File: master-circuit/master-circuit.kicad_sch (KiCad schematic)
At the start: 114 parts, among them U6 20nF 5%

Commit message: Finish master controller circuit, arrange chips on the board.
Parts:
- removed C17, C18, C27, C28, C29: 100nF, Library:C0603, symbol Library:CC0603KRX7R9BB104 Capacitor 100nF
- removed C36, C37, C38, C39: 1uF, Library:C0603, symbol Library:CL10A105KB8NNNC Capacitor 1uF
- removed D5: ~, Library:SOT-23-3_L3.0-W1.7-P0.95-LS2.9-BR, symbol Library:PSM712-LF-T7 ETV/ESD Diodes
- removed FPC1: ~, Library:FPC-SMD_20P-P0.50_XUNPU_FPC-05F-20PH20, symbol Library:FPC-05F-20PH20 Connector 6P 0.5mm spacing FPC
- removed Q1, Q2, Q3, Q4: ~, Library:WDFN-5_L3.1-W3.1-P0.65-BL_1, symbol Library:40N06D MOSFET N-Channel 40A
- removed U10, U11, U12, U13, U14, U15, U16, U9: ~, Library:DHVQFN-16_L3.5-W2.5-P0.50-BL-EP, symbol Library:RS595SXTQW16 Shift Register
- removed U2, U7: ~, Library:WLCSP-6_L1.2-W0.8-P0.40-TL, symbol Library:TCK420G,L3F Gate driver (high side)
- removed U20: ~, Library:VSSOP-10_L3.0-W3.0-P0.50-LS4.9-BL, symbol Library:INA2181A1IDGSR Current amplifier 2x 20V/V
- added C17: 10uF, Library:C1206, symbol Library:CL31A106KBHNNNE Capacitor 10uF
- added C18: 1uF, Library:C0603, symbol Library:CL10A105KB8NNNC Capacitor 1uF
- added C27, C28: 330pF, Library:C0603, symbol Library:CL10C331JB8NNNC Capacitor 330pF
- added D8: ~, Library:SOT-23-3_L3.0-W1.7-P0.95-LS2.9-BR, symbol Library:PSM712-LF-T7 ETV/ESD Diodes
- added D9: ~, Library:SOD-123_L2.7-W1.6-LS3.7-RD-1, symbol Library:B5819W_C8598 Schottky diode
- added I2C1, I2C2: ~, Library:FPC-SMD_6P-P0.50_XUNPU_FPC-05F-6PH20, symbol Library:FPC-05F-6PH20 Connector 6P 0.5mm spacing FPC
- added R38: 5mΩ, Library:R2512 Shunt with Kelvin connections, symbol Library:RLP25FEGMR005 Shunt resistor 5mΩ 1%
- added R39: 1.5kΩ, Library:R0603, symbol Library:0603WAF1501T5E Resistor 1.5kΩ
- added R40: 20kΩ, Library:R0603, symbol Library:0603WAF2002T5E Resistor 20kΩ
- added R41: 47kΩ, Library:R0603, symbol Library:0603WAF4702T5E Resistor 47kΩ
- added U10: ~, Library:QFN-28_L5.0-W5.0-P0.50-TL-EP3.3, symbol Library:CP2102N-A02-GQFN28R USB to UART converter
- added U11: ~, Library:TSSOP-20_L6.5-W4.4-P0.65-LS6.4-BL, symbol Library:INA4181A1IPWR Current amplifier
- added U9: ~, Library:QFN-14_L2.5-W2.5-P0.50-TL-EP1.4, symbol Library:HUSB311BLA USB dual role PD
- added USB2: ~, Library:USB-C-SMD_TYPE-C16PIN, symbol Library:TYPE-C16PIN USB connector
- H1, H2, U19: now not fitted
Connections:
- net +Probe-1: now also U11.4 (IN+1)
- net +Probe-2: now also U11.6 (IN+2)
- net -Probe-1: now also U11.3 (IN±1)
- net -Probe-2: now also U11.7 (IN±2)
- net 3V3: now also C17.2, I2C1.2, I2C2.2, R39.1, U10.6 (VDD), U10.7 (VREGIN), U9.12 (VCONN), U9.13 (VCONN), U9.3 (VDD), U9.4 (VDD)
- net 3V3A: now also U11.5 (VS)
- net BATTERY_CURRENT: now also U11.8 (OUT2)
- net FSPICLK/SPI2_CLK: now also U8.11 (SRCLK)
- net FSPICS0/MEMORY_CS: now also D4.1 (A1)
- net GND: now also C15.1, C16.1, C25.1, C26.1, U8.17 (EP), U8.8 (GND), C17.1, C18.2, C27.1, C28.1, D8.3 (K), I2C1.1, I2C2.1, R41.2, U10.29 (EP), U10.3 (GND), U11.16 (GND), U9.15 (EP), U9.9 (GND), USB2.1 (SHELL), USB2.2 (SHELL), USB2.3 (SHELL), USB2.4 (SHELL), USB2.A1B12 (GND), USB2.B1A12 (GND)
- net I2C1_SCL: now also I2C1.4
- net I2C1_SDA: now also I2C1.3
- net I2C2_SCL: now also I2C2.4, U9.6 (SCL)
- net I2C2_SDA: now also I2C2.3, U9.7 (SDA)
- net REFERENCE: now also U11.1 (REF1), U11.12 (REF3), U11.20 (REF4), U11.9 (REF2)
- net RX: now also U10.26 (TXD)
- net SPI3_CLK: no longer U8.11 (SRCLK)
- net SPI3_MOSI: no longer U8.14 (SER)
- net STATUS_LED: now also U1.28 (IO35); no longer U1.12 (IO8)
- net TX: now also U10.25 (RXD)
- net VBUS_CURRENT: now also U11.2 (OUT1)
- net at C21.2, C22.2, D1.1 (-)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: now also D9.1 (-)
- net at CARD1.8 (DAT1(RSV)), R12.1: no longer D4.1 (A1)
- net I2C1_BOOT0/STOP: now reaches U8.1 (Q1)
- net I2C1_BOOT0/STOP: now also I2C1.6
- net I2C1_NRST: now reaches U8.15 (Q0)
- net I2C1_NRST: now also I2C1.5
- net I2C2_NRST: now reaches U8.2 (Q2)
- net I2C2_NRST: now also I2C2.5
- net I2C2_BOOT0/STOP: now reaches U8.3 (Q3)
- net I2C2_BOOT0/STOP: now also I2C2.6
- net SENSOR_NRST: now reaches U8.4 (Q4)
- net SENSOR_NRST: now also USB2.A8 (SBU1)
- net SENSOR_BOOT0/STOP: now reaches U8.5 (Q5)
- net SENSOR_BOOT0/STOP: now also USB2.B8 (SBU2)
- net CONNECT_SENSORS_5V: now reaches U8.6 (Q6)
- net CONNECT_SENSORS_VCC: now reaches U8.7 (Q7)
- net IMU_INTERRUPT: no longer names the net of U18.11 (INT1)
- net IMU_INTERRUPT: no longer U1.28 (IO35)
- new net: R39.2, U10.9 (RSTb)
- new net: C18.1, R40.2, R41.1, U10.8 (VBUS)
- new net +Probe-3: R38.4 (Probe-2), U11.15 (IN+3)
- new net -Probe-3: R38.3 (Probe-1), U11.14 (IN±3)
- new net SENSORS_CC1: C27.2, U9.10 (CC1), U9.11 (CC1), USB2.A5 (CC1)
- new net SENSORS_CC2: C28.2, U9.1 (CC2), U9.14 (CC2), USB2.B5 (CC2)
- new net SENSORS_USB_D+: D8.2 (A1), U10.4 (D+), USB2.A6 (DP1), USB2.B6 (DP2)
- new net SENSORS_USB_D-: D8.1 (A1), U10.5 (D-), USB2.A7 (DN1), USB2.B7 (DN2)
- new net SENSORS_VBUS: R38.1 (Shunt-1), R40.1, U9.2 (VBUS)
- new net SENSORS_VBUS_PINS: D9.2 (+), R38.2 (Shunt-2), USB2.A4B9 (VBUS), USB2.B4A9 (VBUS)
- new net SENSOR_CURRENT: U1.12 (IO8), U11.13 (OUT3)
- new net SHIFT_BANK_2_DATA_CONT: U8.14 (SER)
- no-connect marks 19 -> 52
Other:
- added sheet back-to-back-mosfets (back-to-back-mosfets.kicad_sch)
- added sheet back-to-back-mosfets1 (back-to-back-mosfets.kicad_sch)
- added sheet back-to-back-mosfets2 (back-to-back-mosfets.kicad_sch)
- added sheet back-to-back-mosfets3 (back-to-back-mosfets.kicad_sch)
- added sheet group-of-8-servo-connectors (group-of-8-servo-connectors.kicad_sch)
- added sheet group-of-8-servo-connectors1 (group-of-8-servo-connectors.kicad_sch)
- added sheet group-of-8-servo-connectors2 (group-of-8-servo-connectors.kicad_sch)
- note added: "Eusebiu - USB C - The guest"
- note added: "Eusebiu - USB C - The host"
- note added: "Ground the shell for an upstream device."
- note added: "I2C connectors and battery level LEDs"
- note added: "Note: pullups included in ESP32-S3 series."
- note added: "SBU1 and SBU2 are coonected to Reset and Boot0 pins for the mini drive."
- note added: "SDA A FPC connector"
- note added: "SDA B FPC connector"
- note removed: "Back to back N-Channel MOSFET configuration to stop current in both directions."
- note removed: "Boot buttons and voltage monitor"
- note removed: "Eusebiu - USB C"
- note removed: "Note: pullup resistors are included in ESP32-S3 series."
- note removed: "Power and control, FPC connector"
- title: Master motor control circuit -> Hex master motor control circuit
- moved on the sheet: C1, C10, C11, C12, C13, C14, C19, C2, C20, C21, C22, C23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
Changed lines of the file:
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@@
 	(generator "eeschema")
 	(generator_version "9.0")
-	(paper "A1")
+	(paper "A2")
 	(title_block
-		(title "Master motor control circuit")
+		(title "Hex master motor control circuit")
 		(company "Hex Robotics Limited")
 		(comment 1 "Author: Calin Mocanu")

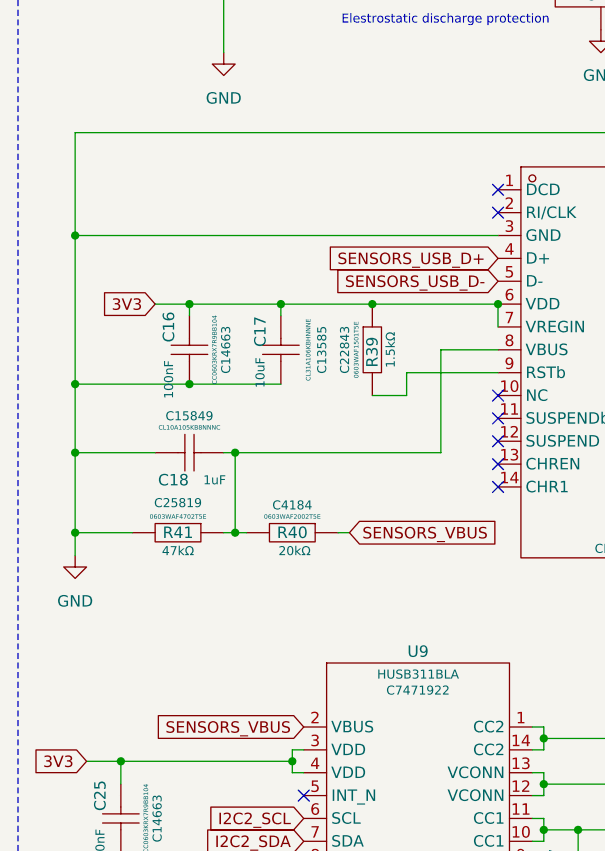
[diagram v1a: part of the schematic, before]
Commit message: Partially wire up control circuit.
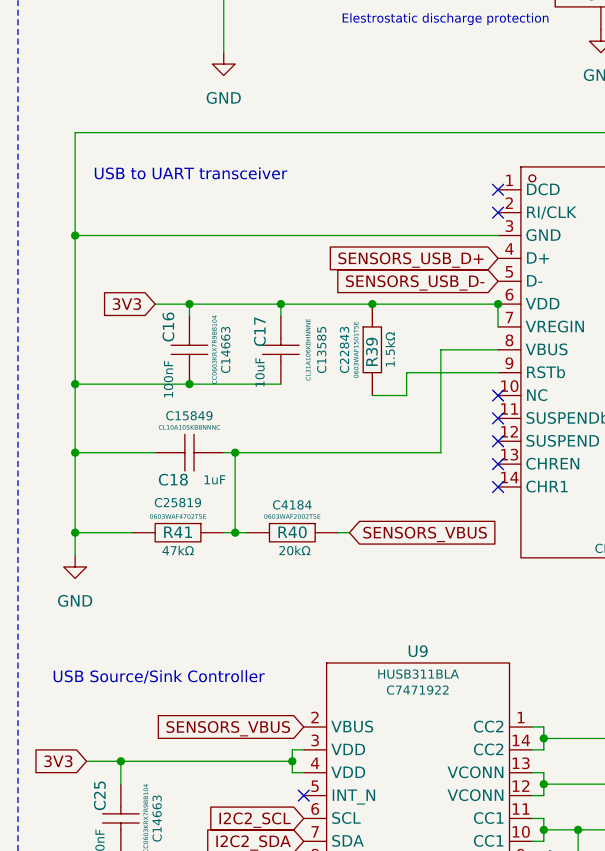
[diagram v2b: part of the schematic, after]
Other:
- note added: "USB Source/Sink Controller"
- note added: "USB to UART transceiver"

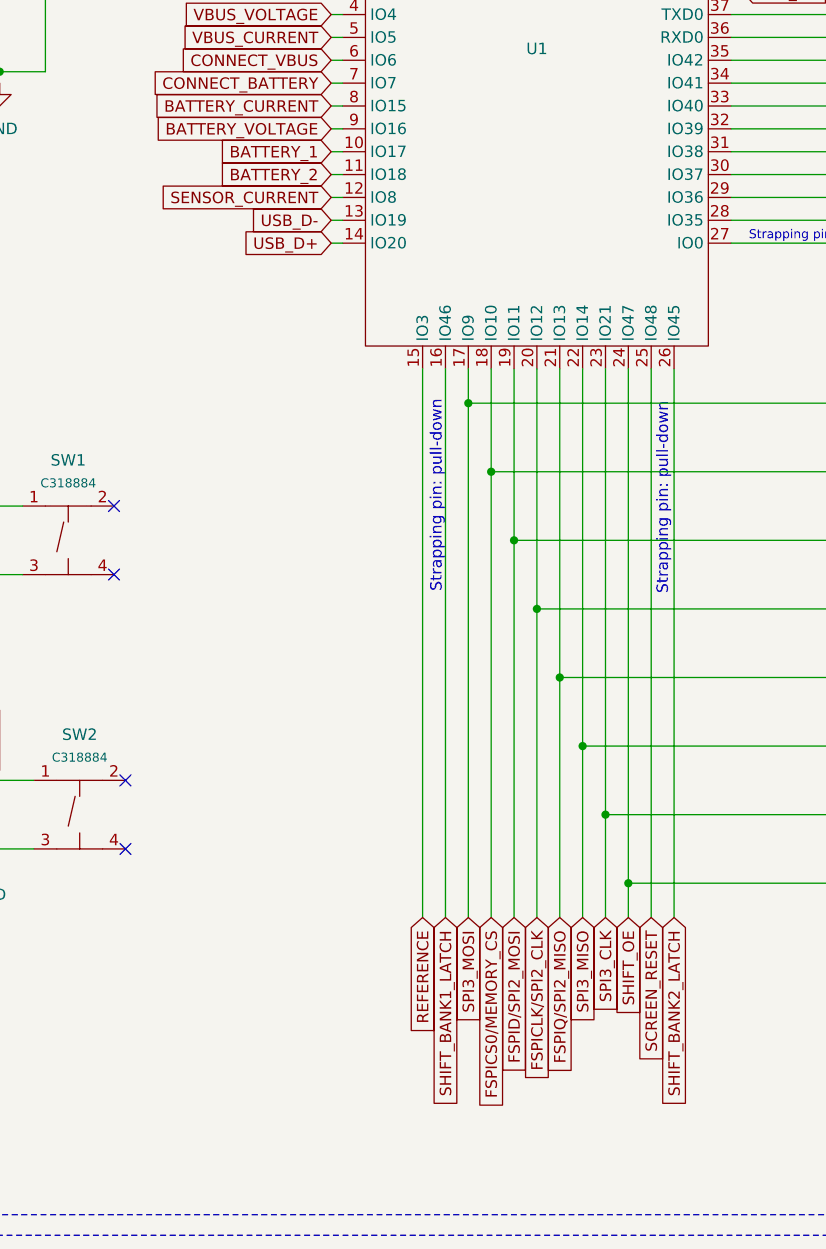
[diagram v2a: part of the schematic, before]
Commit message: Continue wiring control circuit.
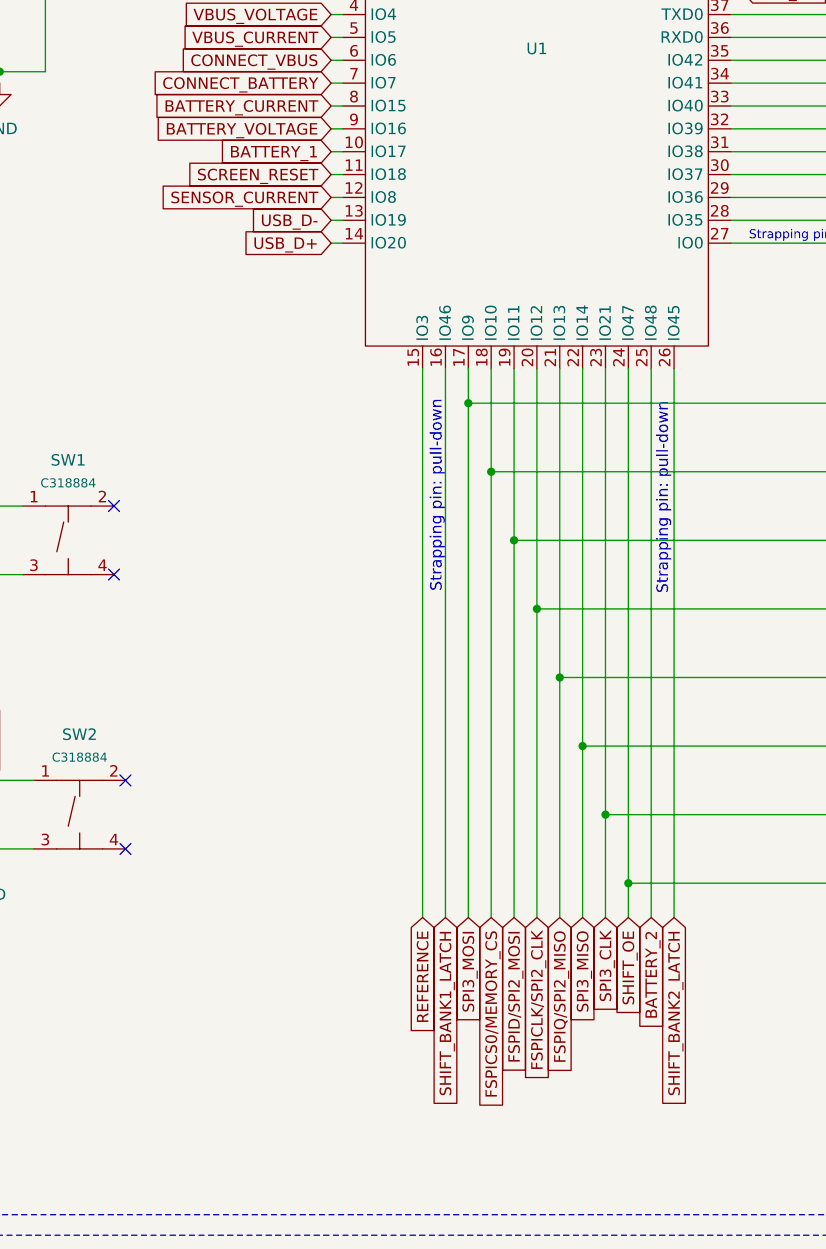
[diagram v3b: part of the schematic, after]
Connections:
- net BATTERY_2: now also U1.25 (IO48); no longer U1.11 (IO18)
- net SCREEN_RESET: now also U1.11 (IO18); no longer U1.25 (IO48)

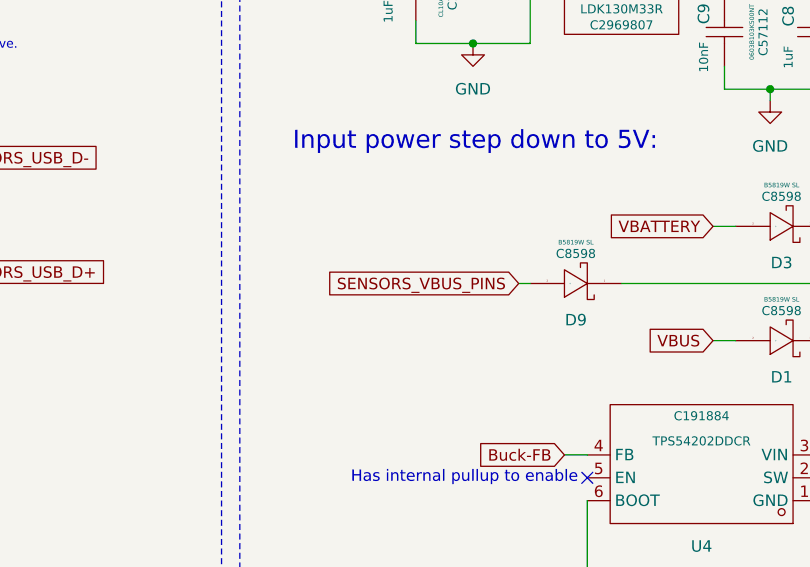
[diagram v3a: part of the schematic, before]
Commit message: Complete wiring up control circuit (needs verifying).
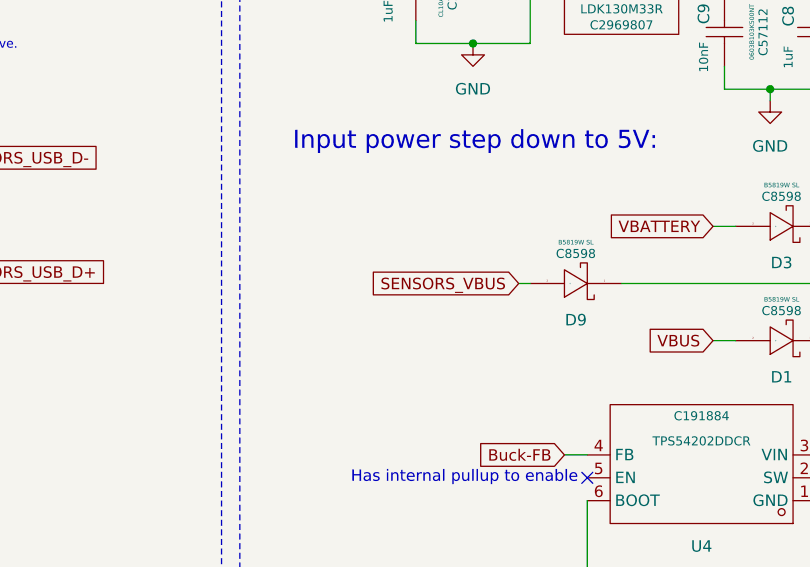
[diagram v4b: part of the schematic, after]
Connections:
- net SENSORS_VBUS: now also D9.2 (+)
- net SENSORS_VBUS_PINS: no longer D9.2 (+)

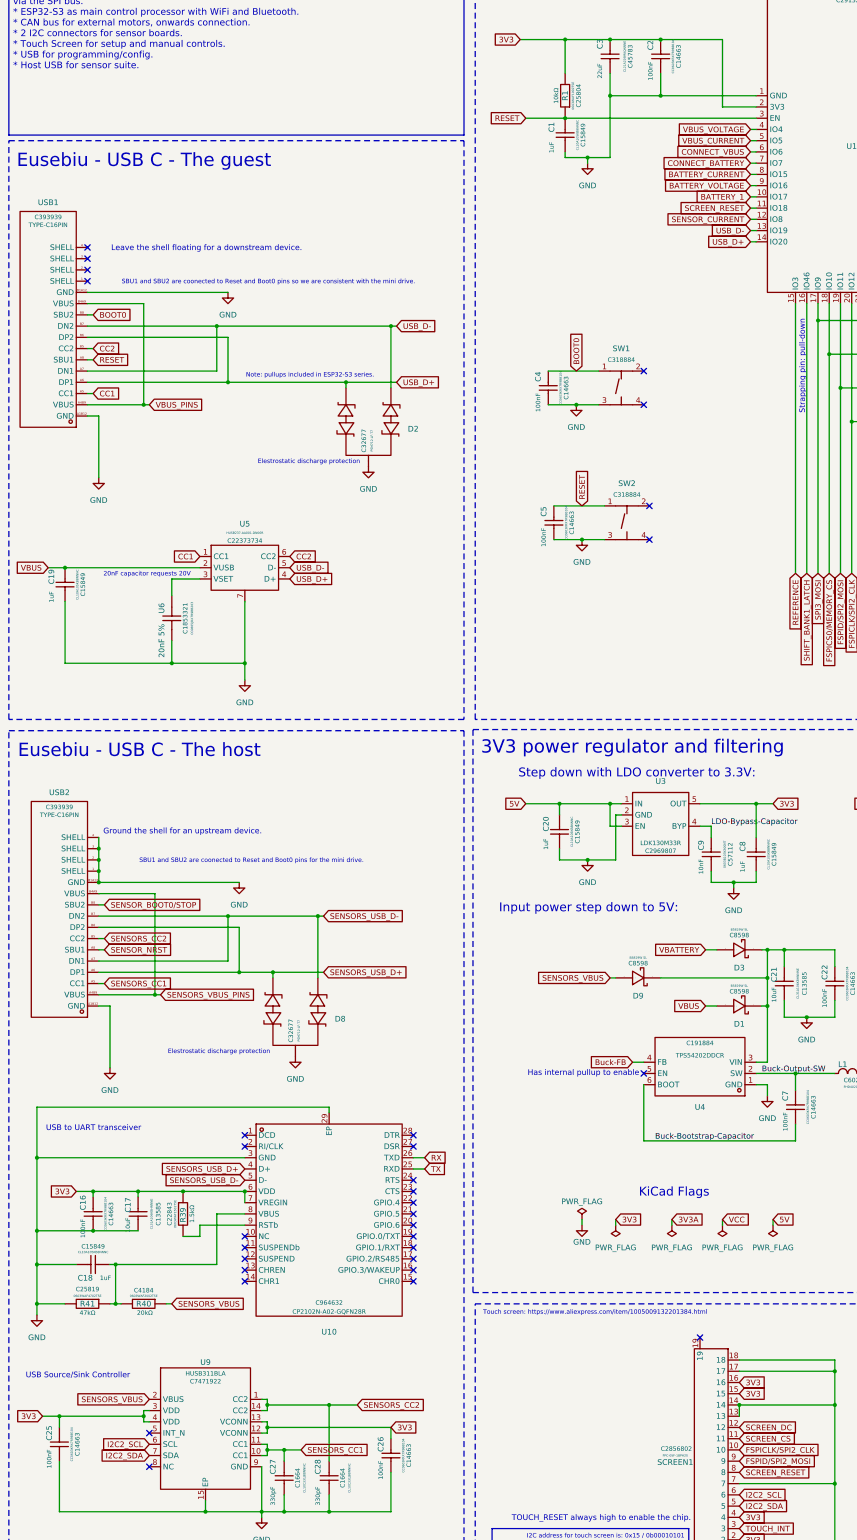
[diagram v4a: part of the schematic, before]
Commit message: Compile and test master circuit for liveness. It lives!
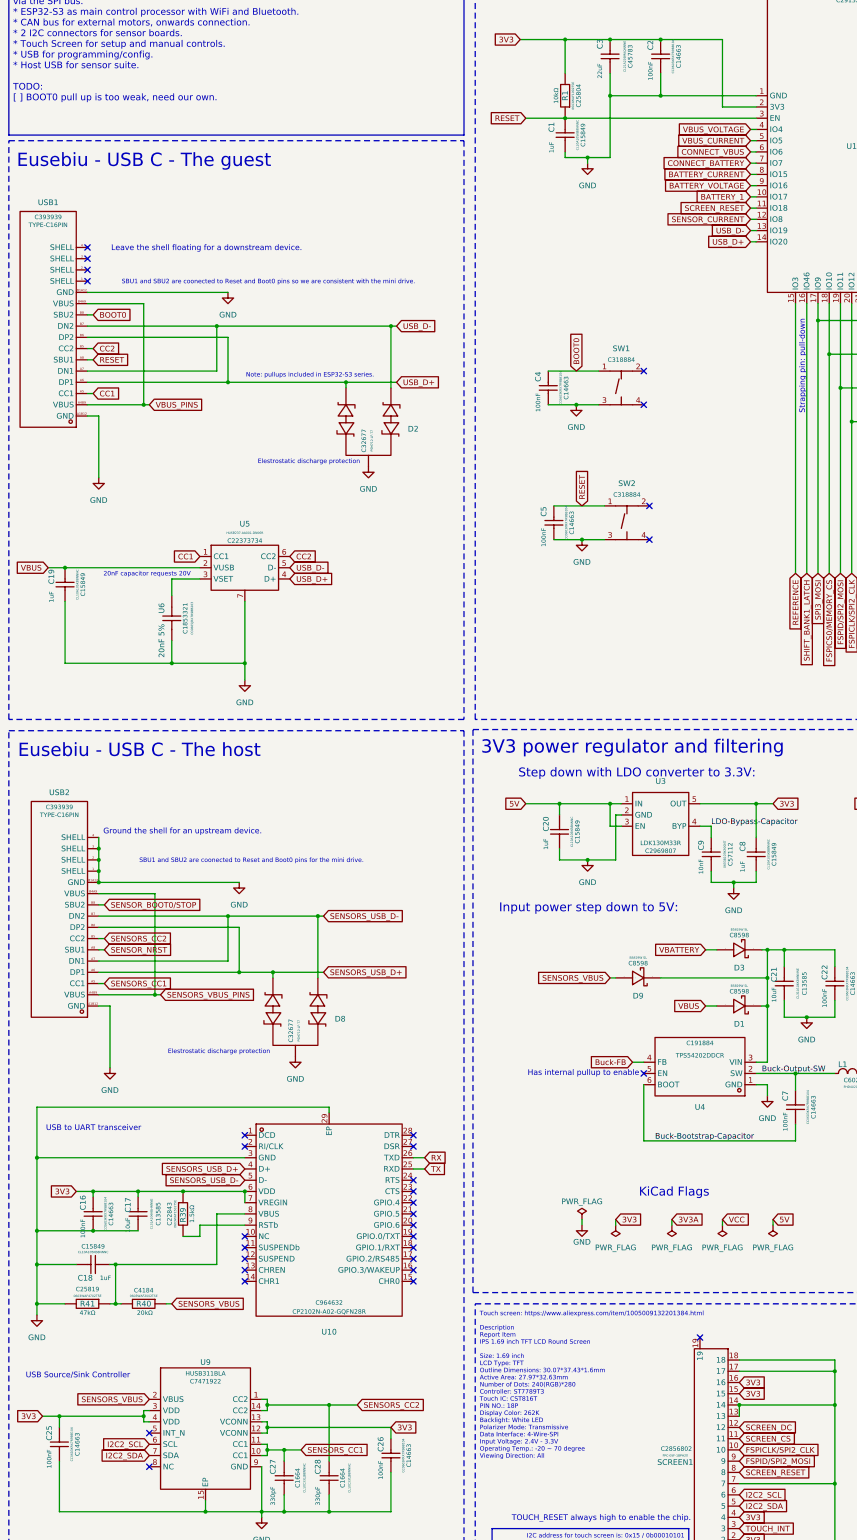
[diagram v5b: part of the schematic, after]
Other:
- note added: "Touch screen: https://www.aliexpress.com/item/1005009132201384.html Description Report Item IPS 1.69 inch TFT LCD Round Screen Size: 1.69 inch LCD Type: TFT Outline Dimensions: 30.07*37.43*1.6mm Active Area: 27.97*32.63mm Number of Dots: 240(RGB)*280 Controller: ST7789T3 Touch IC: CST816T PIN NO.: 18P Display Color: 262K Backlight: White LED Polarizer Mode: Transmissive Data Interface: 4-Wire-SPI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"
- note removed: "Touch screen: https://www.aliexpress.com/item/1005009132201384.html"
